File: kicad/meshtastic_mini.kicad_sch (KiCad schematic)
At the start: 8 parts, among them U1 ESP32-C3_SuperMini, U2 RFM95W-868S2

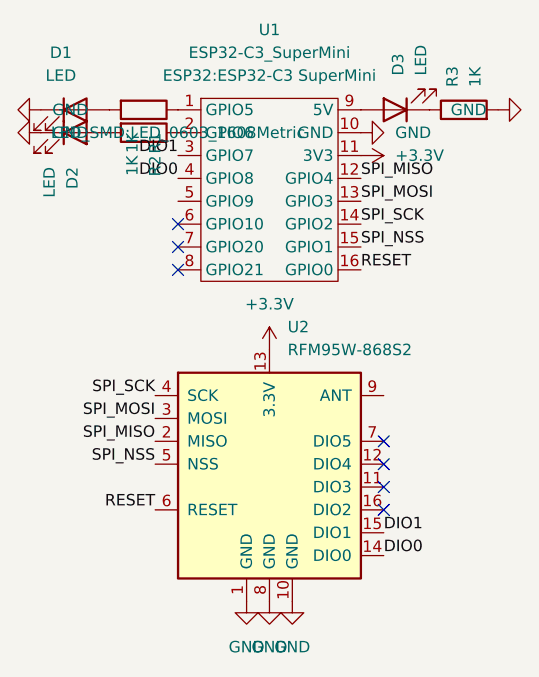
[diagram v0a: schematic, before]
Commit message: connected DIO0 to pin 10 instead of 9
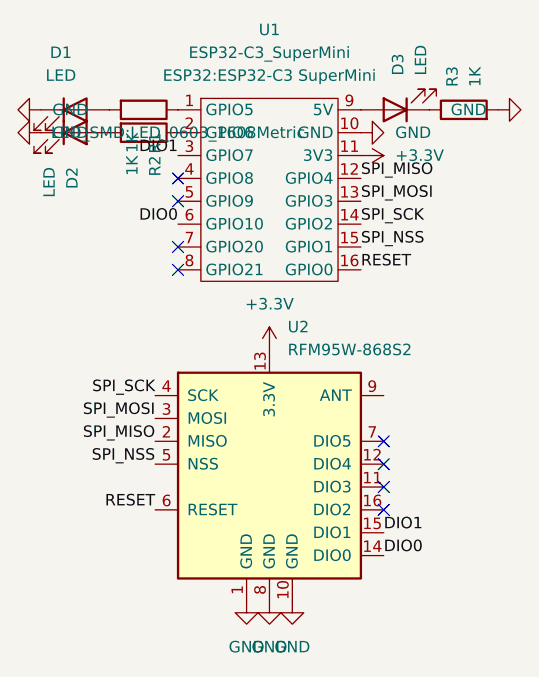
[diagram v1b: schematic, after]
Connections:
- net DIO0: now also U1.6 (GPIO10); no longer U1.4 (GPIO8)
- no-connect marks 7 -> 8
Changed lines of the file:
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@@
   (paper "A4")
   (no_connect (at 152.4 127))
-  (no_connect (at 129.54 102.87))
+  (no_connect (at 129.54 100.33))
   (no_connect (at 129.54 107.95))
   (no_connect (at 152.4 129.54))
@@
   (no_connect (at 152.4 132.08))
   (no_connect (at 152.4 134.62))
+  (no_connect (at 129.54 97.79))
   (label "SPI_MISO" (at 149.86 97.79 0)
     (effects (font (size 1.27 1.27)) (justify left bottom))
@@
     (effects (font (size 1.27 1.27)) (justify right bottom))
   )
-  (label "DIO0" (at 129.54 97.79 180)
+  (label "DIO0" (at 129.54 102.87 180)
     (effects (font (size 1.27 1.27)) (justify right bottom))
   )

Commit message: fixed third LED wiring (that noone will probably ever use)
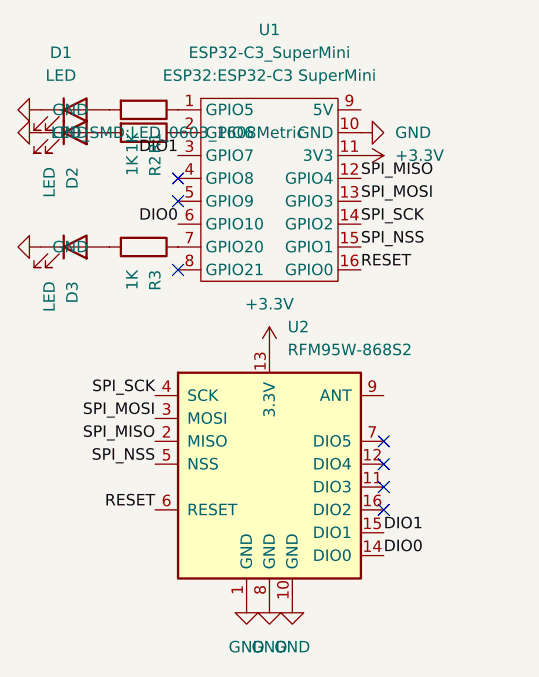
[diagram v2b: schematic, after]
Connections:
- net GND: now also D3.1 (K); no longer R3.2
- net at U1.7 (GPIO20): now also R3.1
- net at U1.9 (5V): no longer D3.2 (A)
- new net: D3.2 (A), R3.2
- no-connect marks 8 -> 7
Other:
- moved on the sheet: D3, R3

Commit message: adapted for usage with XIAO nrf52 module
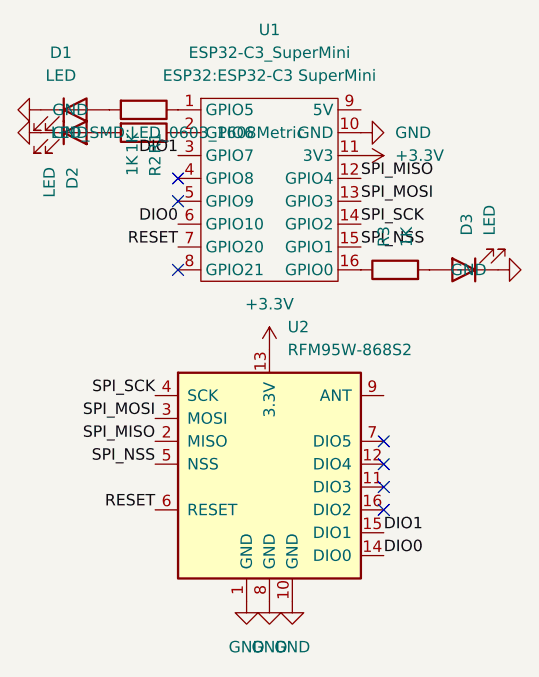
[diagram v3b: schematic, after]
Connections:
- net RESET: now also U1.7 (GPIO20); no longer U1.16 (GPIO0)
- net at R3.1: now also U1.16 (GPIO0); no longer U1.7 (GPIO20)
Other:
- moved on the sheet: D3, R3
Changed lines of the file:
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@@
 		(at 129.54 97.79)
+	)
+	(label "RESET"
+		(at 129.54 105.41 180)
+		(effects
+			(font
+				(size 1.27 1.27)
+			)
+			(justify right bottom)
+		)
 	)
 	(label "SPI_MISO"
@@
 		)
 	)
-	(label "RESET"
-		(at 149.86 107.95 0)
-		(effects
-			(font
-				(size 1.27 1.27)
-			)
-			(justify left bottom)
-		)
-	)
 	(label "SPI_NSS"
 		(at 127 129.54 180)
@@
 	(symbol
 		(lib_id "Device:LED")
-		(at 118.11 105.41 0)
+		(at 161.29 107.95 180)
 		(unit 1)
 		(exclude_from_sim no)
@@
 		(fields_autoplaced yes)
 		(property "Reference" "D3"
-			(at 117.7926 109.22 90)
+			(at 161.6074 104.14 90)
 			(effects
 				(font
@@
 		)
 		(property "Value" "LED"
-			(at 115.2526 109.22 90)
+			(at 164.1474 104.14 90)
 			(effects
 				(font
@@
 		)
 		(property "Footprint" "LED_SMD:LED_0603_1608Metric"
-			(at 118.11 105.41 0)
+			(at 161.29 107.95 0)
 			(effects
 				(font
@@
 		)
 		(property "Datasheet" "~"
-			(at 118.11 105.41 0)
-			(effects
-				(font
-					(size 1.27 1.27)
-				)
-				(hide yes)
-			)
-		)
-		(property "Description" ""
-			(at 118.11 105.41 0)
+			(at 161.29 107.95 0)
+			(effects
+				(font
+					(size 1.27 1.27)
+				)
+				(hide yes)
+			)
+		)
+		(property "Description" ""
+			(at 161.29 107.95 0)
 			(effects
 				(font
@@
 	(symbol
 		(lib_id "power:GND")
-		(at 114.3 105.41 270)
+		(at 165.1 107.95 90)
 		(unit 1)
 		(exclude_from_sim no)
@@
 		(fields_autoplaced yes)
 		(property "Reference" "#PWR0108"
-			(at 107.95 105.41 0)
+			(at 171.45 107.95 0)
 			(effects
 				(font
@@
 		)
 		(property "Value" "GND"
-			(at 115.57 105.4099 90)
+			(at 163.83 107.9501 90)
 			(effects
 				(font
@@
 		)
 		(property "Footprint" ""
-			(at 114.3 105.41 0)
+			(at 165.1 107.95 0)
 			(effects
 				(font
@@
 		)
 		(property "Datasheet" ""
-			(at 114.3 105.41 0)
-			(effects
-				(font
-					(size 1.27 1.27)
-				)
-				(hide yes)
-			)
-		)
-		(property "Description" ""
-			(at 114.3 105.41 0)
+			(at 165.1 107.95 0)
+			(effects
+				(font
+					(size 1.27 1.27)
+				)
+				(hide yes)
+			)
+		)
+		(property "Description" ""
+			(at 165.1 107.95 0)
 			(effects
 				(font
@@
 	(symbol
 		(lib_id "Device:R")
-		(at 125.73 105.41 270)
+		(at 153.67 107.95 90)
 		(unit 1)
 		(exclude_from_sim no)
@@
 		(fields_autoplaced yes)
 		(property "Reference" "R3"
-			(at 127.0001 107.95 0)
+			(at 152.3999 105.41 0)
 			(effects
 				(font
@@
 		)
 		(property "Value" "1K"
-			(at 124.4601 107.95 0)
+			(at 154.9399 105.41 0)
 			(effects
 				(font
@@
 		)
 		(property "Footprint" "Resistor_SMD:R_0402_1005Metric"
-			(at 125.73 103.632 90)
+			(at 153.67 109.728 90)
 			(effects
 				(font
@@
 		)
 		(property "Datasheet" "~"
-			(at 125.73 105.41 0)
-			(effects
-				(font
-					(size 1.27 1.27)
-				)
-				(hide yes)
-			)
-		)
-		(property "Description" ""
-			(at 125.73 105.41 0)
-			(effects
-				(font
+			(at 153.67 107.95 0)
+			(effects
+				(font
+					(size 1.27 1.27)
+				)
+				(hide yes)
+			)
+		)
+		(property "Description" ""
+			(at 153.67 107.95 0)
+			(effects
+				(font
